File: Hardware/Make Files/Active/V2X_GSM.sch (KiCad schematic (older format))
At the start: 46 parts, among them P1 47553-1001, P14 CUR_SEN, P2 SMA, P26 CONN_02X08, P3 SMA, Q12 IRF9335, U13 XRP6124, U3 MMQA5V6T3G, U4 SIM5320

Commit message: work from home day
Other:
- moved on the sheet: C23, C24, C25, C26, C27, C28, FB3, P26, R84, R85, R86

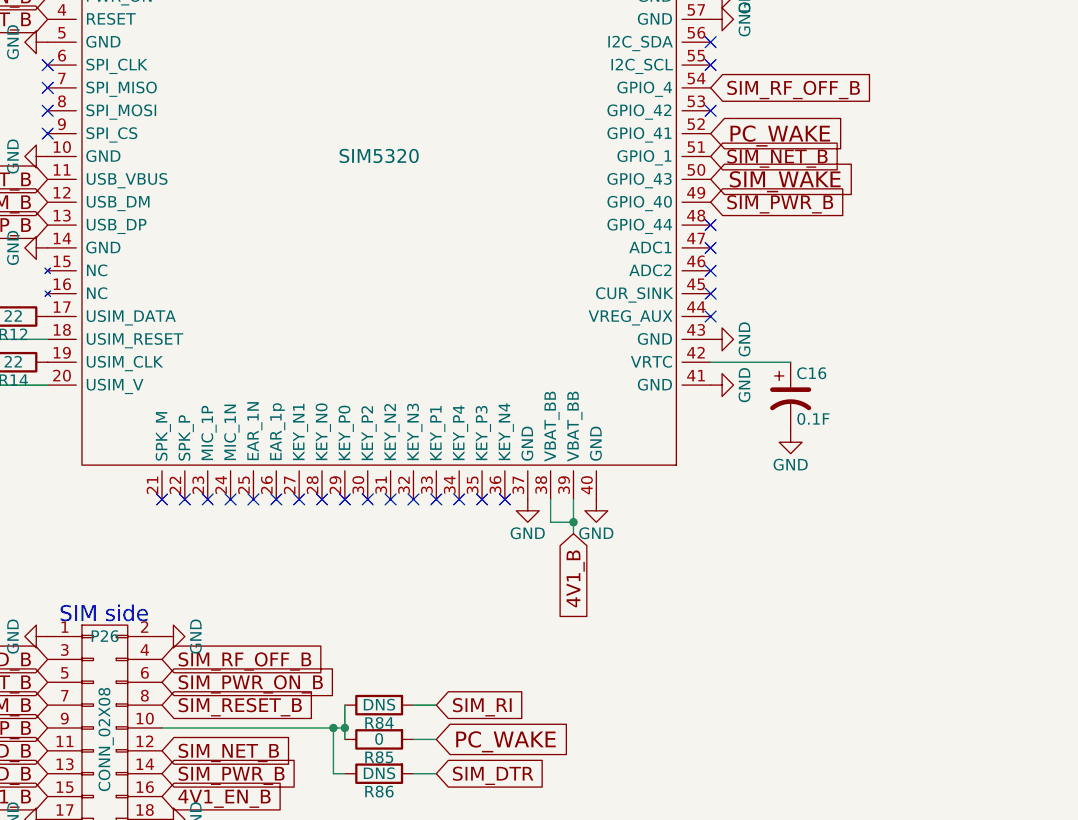
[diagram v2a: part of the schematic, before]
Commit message: Verification findings and modifications
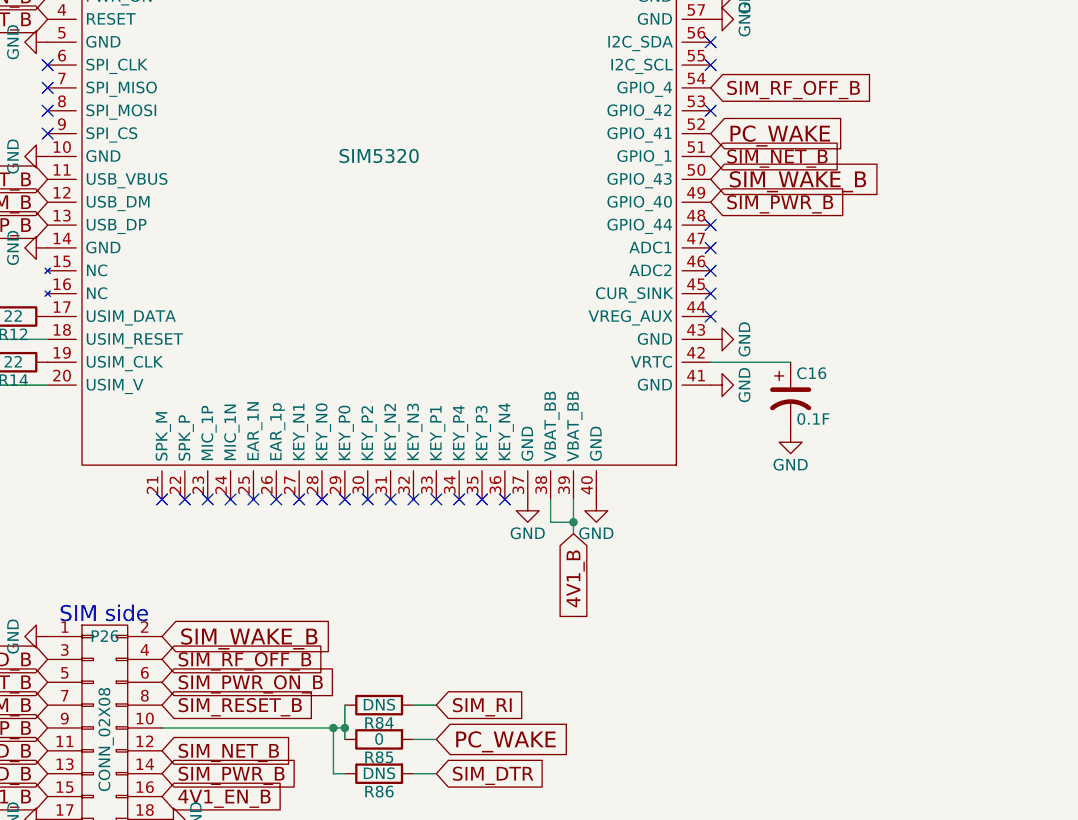
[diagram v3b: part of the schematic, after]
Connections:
- net GND: no longer P26.2 (P2)
- net SIM_WAKE renamed SIM_WAKE_B
- net SIM_WAKE_B: now also P26.2 (P2)

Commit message: BOM updates
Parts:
- C15: Mouse PN 77-VJ0603A331FXXCB -> 80-C0603C331J5G
- C17, C19: Mouse PN 77-VJ0603A331FXXCB -> 77-VJ0603D331KXAAJ
- C21, C22: Mouse PN (none) -> 80-CBR06C470J5G
- C24, C28: Mouse PN 963-LMK212B7475KG-T -> 581-12063C475KAT2A
- P1: value 47553-1001 -> SIM_SKT
- P26: value CONN_02X08 -> CONN_02X10
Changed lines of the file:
@@
 P 9850 1350
 F 0 "P1" H 9850 1900 50  0000 C CNN
-F 1 "47553-1001" V 9950 1350 50  0000 C CNN
+F 1 "SIM_SKT" V 9950 1350 50  0000 C CNN
 F 2 "Custom Parts:47553-1001" H 9850 1350 60  0001 C CNN
 F 3 "http://www.mouser.com/ds/2/276/0475531001_MEMORY_CARD_SOCKET-146294.pdf" H 9850 1350 60  0001 C CNN
@@
 F 1 "330P" H 7275 4950 50  0000 L CNN
 F 2 "Custom Parts:C_0603_SM" H 7288 4900 30  0001 C CNN
-F 3 "http://www.mouser.com/ds/2/427/vjw1bcbascomseries-223529.pdf" H 7250 5050 60  0001 C CNN
-F 4 "77-VJ0603A331FXXCB" H 7250 5050 60  0001 C CNN "Mouse PN"
+F 3 "http://www.mouser.com/ds/2/427/vjhifreq-109303.pdf" H 7250 5050 60  0001 C CNN
+F 4 "77-VJ0603D331KXAAJ" H 7250 5050 60  0001 C CNN "Mouse PN"
 	1    7250 5050
 	-1   0    0    1
@@
 F 2 "Custom Parts:C_0805_SM" H 2338 6100 30  0001 C CNN
 F 3 "http://www.yuden.co.jp/productdata/catalog/en/mlcc_all_e.pdf" H 2300 6250 60  0001 C CNN
-F 4 "963-LMK212B7475KG-T" H 2300 6250 60  0001 C CNN "Mouse PN"
+F 4 "581-12063C475KAT2A" H 2300 6250 60  0001 C CNN "Mouse PN"
 	1    2300 6250
 	-1   0    0    -1
@@
 F 2 "Custom Parts:C_0805_SM" H 4188 6100 30  0001 C CNN
 F 3 "http://www.yuden.co.jp/productdata/catalog/en/mlcc_all_e.pdf" H 4150 6250 60  0001 C CNN
-F 4 "963-LMK212B7475KG-T" H 4150 6250 60  0001 C CNN "Mouse PN"
+F 4 "581-12063C475KAT2A" H 4150 6250 60  0001 C CNN "Mouse PN"
 	1    4150 6250
 	-1   0    0    -1
@@
 F 1 "330P" H 9275 3000 50  0000 L CNN
 F 2 "Custom Parts:C_0603_SM" H 9288 2950 30  0001 C CNN
-F 3 "http://www.mouser.com/ds/2/427/vjw1bcbascomseries-223529.pdf" H 9250 3100 60  0001 C CNN
-F 4 "77-VJ0603A331FXXCB" H 9250 3100 60  0001 C CNN "Mouse PN"
+F 3 "http://www.mouser.com/ds/2/212/KEM_C1003_C0G_SMD-356956.pdf" H 9250 3100 60  0001 C CNN
+F 4 "80-C0603C331J5G" H 9250 3100 60  0001 C CNN "Mouse PN"
 	1    9250 3100
 	-1   0    0    -1
@@
 F 1 "47p" H 9375 5550 50  0000 L CNN
 F 2 "Custom Parts:C_0603_SM" H 9388 5500 30  0001 C CNN
-F 3 "" H 9350 5650 60  0000 C CNN
+F 3 "http://www.mouser.com/ds/2/212/KEM_C1030_CBR_SMD-346920.pdf" H 9350 5650 60  0001 C CNN
+F 4 "80-CBR06C470J5G" H 9350 5650 60  0001 C CNN "Mouse PN"
 	1    9350 5650
 	0    -1   -1   0
@@
 P 2200 5100
 F 0 "P26" H 2200 5550 50  0000 C CNN
-F 1 "CONN_02X08" V 2200 5100 50  0000 C CNN
+F 1 "CONN_02X10" V 2200 5100 50  0000 C CNN
 F 2 "Pin_Headers:Pin_Header_Straight_2x10" H 2200 3900 60  0001 C CNN
 F 3 "http://www.mouser.com/ProductDetail/FCI/77313-824-20LF/?qs=sGAEpiMZZMs%252bGHln7q6pm24n0txessAMJKIe4p3QHSo%3d" H 2200 3900 60  0001 C CNN
@@
 F 1 "47p" H 7525 5550 50  0000 L CNN
 F 2 "Custom Parts:C_0603_SM" H 7538 5500 30  0001 C CNN
-F 3 "" H 7500 5650 60  0000 C CNN
+F 3 "http://www.mouser.com/ds/2/212/KEM_C1030_CBR_SMD-346920.pdf" H 7500 5650 60  0001 C CNN
+F 4 "80-CBR06C470J5G" H 7500 5650 60  0001 C CNN "Mouse PN"
 	1    7500 5650
 	0    -1   -1   0
@@
 F 1 "330P" H 9275 4950 50  0000 L CNN
 F 2 "Custom Parts:C_0603_SM" H 9288 4900 30  0001 C CNN
-F 3 "http://www.mouser.com/ds/2/427/vjw1bcbascomseries-223529.pdf" H 9250 5050 60  0001 C CNN
-F 4 "77-VJ0603A331FXXCB" H 9250 5050 60  0001 C CNN "Mouse PN"
+F 3 "http://www.mouser.com/ds/2/427/vjhifreq-109303.pdf" H 9250 5050 60  0001 C CNN
+F 4 "77-VJ0603D331KXAAJ" H 9250 5050 60  0001 C CNN "Mouse PN"
 	1    9250 5050
 	-1   0    0    1

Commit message: V1.2 Ordered
This is a capture of the project folder at the time f ordering the V1.2
kit.
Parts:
- removed C22: 47p, Custom Parts:C_0603_SM, symbol C
- removed L6, L7: 47N, Custom Parts:C_0603_SM, symbol INDUCTOR_SMALL
- added U24: TLV70012DCK, symbol TLV70012DCK
- C17: value 330P -> 56P; Mouse PN 77-VJ0603D331KXAAJ -> 581-08052U560G
- C18: value 10N -> 470P; Mouse PN 77-VJ0603Y103KXACBC -> 77-VJ0603D471KXXAJ
- C19: value 330P -> 100N; Mouse PN 77-VJ0603D331KXAAJ -> 810-C1608X7R1E104K
- C20: value 10N -> 4U7; footprint Custom Parts:C_0603_SM -> Custom Parts:C_0805_SM; Mouse PN 77-VJ0603Y103KXACBC -> 581-12063C475KAT2A
- C21: value 47p -> 150p; Mouse PN 80-CBR06C470J5G -> 77-VJ0805Q151JXAAC
- L1: value 47N -> 330N
- L2: value 47N -> 120N; Mouse PN 81-LQG18HN47NJ00D -> 81-LQW18CNR12J00D
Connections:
- net GSM is gone; now on net GSM_ANT: P3.1 (P1)
- net 4V1F1: now also C19.1, U24.1 (IN), U24.3 (EN); no longer L1.1
- net GND: now also C17.2, C19.2, U24.2 (GND); no longer C17.1, C19.1
- net at C18.1, L1.2, L2.2: now also C17.1; no longer C17.2
- net 3V3F1: now reaches C20.1
- net 3V3F1: now also L1.1, U24.5 (OUT); no longer C19.2
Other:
- moved on the sheet: C17, C18, C21, L1, L2, P2, P3

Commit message: Added learnings from V1.2 build
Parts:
- C47: footprint Custom Parts:C_0805_SM -> Custom Parts:C_1206_SM
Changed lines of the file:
@@
 F 0 "C47" H 3575 7250 50  0000 L CNN
 F 1 "4U7" H 3575 7050 50  0000 L CNN
-F 2 "Custom Parts:C_0805_SM" H 3588 7000 30  0001 C CNN
+F 2 "Custom Parts:C_1206_SM" H 3588 7000 30  0001 C CNN
 F 3 "http://www.mouser.com/ds/2/40/cx7r-218113.pdf" H 3550 7150 60  0001 C CNN
 F 4 "581-12063C475KAT2A" H 3550 7150 60  0001 C CNN "Mouse PN"
@@
 F 0 "U24" H 7350 4800 40  0000 C CNN
 F 1 "TLV70012DCK" H 7700 4800 40  0000 C CNN
-F 2 "" H 7600 4700 35  0000 C CIN
+F 2 "" H 7600 4700 35  0001 C CIN
 F 3 "" H 7600 4600 60  0000 C CNN
 	1    7600 4600

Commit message: V2X Build learnings
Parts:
- removed R8, R9: DNS, Custom Parts:R_0603_sm, symbol R
- P26: Mouse PN 649-77313-824-20LF -> 571-2-84952-0
- U24: footprint (none) -> TO_SOT_Packages_SMD:SOT-23-5
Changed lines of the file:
@@
 	0    1    1    0
-$EndComp
-$Comp
-L R R8
-U 1 1 55A75EF8
-P 8750 1550
-F 0 "R8" V 8830 1550 50  0000 C CNN
-F 1 "DNS" V 8750 1550 50  0000 C CNN
-F 2 "Custom Parts:R_0603_sm" V 8680 1550 30  0001 C CNN
-F 3 "" H 8750 1550 30  0000 C CNN
-	1    8750 1550
-	-1   0    0    1
 $EndComp
 Text GLabel 9450 2950 2    60   Input ~ 0
@@
 	9650 1200 9650 1200
 Connection ~ 9650 1800
-Wire Wire Line
-	9650 1700 9650 2000
 Connection ~ 4250 4150
 Wire Wire Line
@@
 	2300 6100 2300 6050
 Connection ~ 2300 6050
-Text GLabel 8650 1350 0    60   Input ~ 0
-4V1_B
-$Comp
-L R R9
-U 1 1 5602F7C8
-P 8750 1850
-F 0 "R9" V 8830 1850 50  0000 C CNN
-F 1 "DNS" V 8750 1850 50  0000 C CNN
-F 2 "Custom Parts:R_0603_sm" V 8680 1850 30  0001 C CNN
-F 3 "" H 8750 1850 30  0000 C CNN
-	1    8750 1850
-	-1   0    0    1
-$EndComp
-Wire Wire Line
-	9650 1600 8950 1600
-Wire Wire Line
-	8950 1600 8950 1700
-Wire Wire Line
-	8950 1700 8650 1700
-Wire Wire Line
-	8750 1350 8650 1350
-Wire Wire Line
-	8750 1350 8750 1400
-Connection ~ 8750 1700
 Text GLabel 4850 2450 2    69   Input ~ 0
 PC_WAKE
@@
 	-1   0    0    -1
 $EndComp
-Wire Wire Line
-	9650 2000 8750 2000
 $Comp
 L C C15
@@
 F 1 "CONN_02X10" V 2200 5100 50  0000 C CNN
 F 2 "Pin_Headers:Pin_Header_Straight_2x10" H 2200 3900 60  0001 C CNN
-F 3 "http://www.mouser.com/ProductDetail/FCI/77313-824-20LF/?qs=sGAEpiMZZMs%252bGHln7q6pm24n0txessAMJKIe4p3QHSo%3d" H 2200 3900 60  0001 C CNN
-F 4 "649-77313-824-20LF" H 2200 5100 60  0001 C CNN "Mouse PN"
+F 3 "http://www.mouser.com/ds/2/418/NG_CD_84952_A4-635383.pdf" H 2200 3900 60  0001 C CNN
+F 4 "571-2-84952-0" H 2200 5100 60  0001 C CNN "Mouse PN"
 	1    2200 5100
 	1    0    0    -1
@@
 Text GLabel 1950 4750 0    60   Input ~ 0
 SIMCARD_B
-Text GLabel 8650 1700 0    60   Input ~ 0
+Text GLabel 9650 1600 0    60   Input ~ 0
 SIMCARD_B
 $Comp
@@
 F 0 "U24" H 7350 4800 40  0000 C CNN
 F 1 "TLV70012DCK" H 7700 4800 40  0000 C CNN
-F 2 "" H 7600 4700 35  0001 C CIN
+F 2 "TO_SOT_Packages_SMD:SOT-23-5" H 7600 4700 35  0001 C CIN
 F 3 "" H 7600 4600 60  0000 C CNN
 	1    7600 4600
@@
 	-1   0    0    -1
 $EndComp
+Wire Wire Line
+	9650 1700 9650 1800
 $EndSCHEMATC
